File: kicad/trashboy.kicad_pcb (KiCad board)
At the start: 2 copper layers, 75 x 67 mm, 29 parts, among them J1 Conn_01x02, J2 Conn_01x07_Socket, U1 MCP23017x-x-SP, X1 TERMBLOCK_1X2

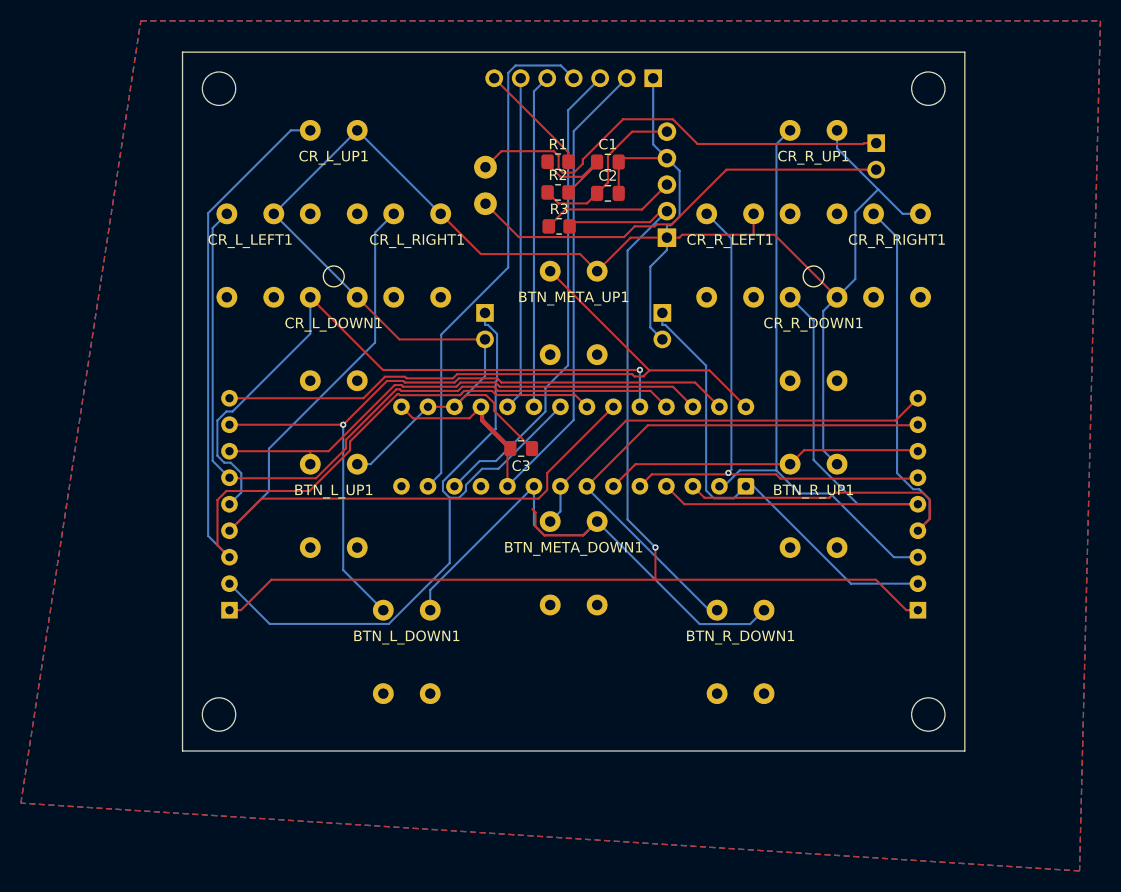
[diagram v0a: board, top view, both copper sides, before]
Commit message: Fix a few PCB issues:
1) 3v3 label issue
2) Reversed polarity on port expander.
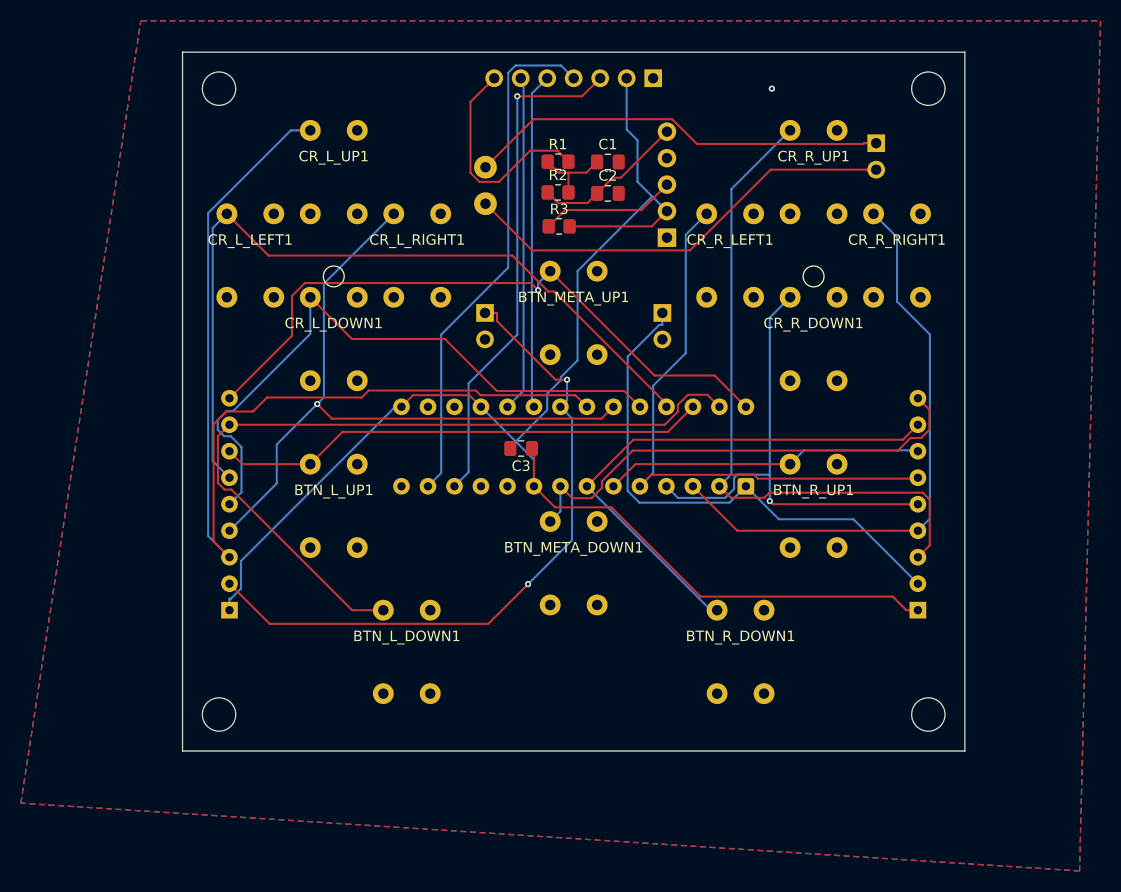
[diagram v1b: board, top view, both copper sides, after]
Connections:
- C3 pad 1: GND -> +3.3V
- C3 pad 2: +3.3V -> GND
- JP1 pad 2: +3V3 -> +3.3V
- R3 pad 2: +3V3 -> +3.3V
- RN1 pad 1: +3V3 -> +3.3V
- RN2 pad 1: +3V3 -> +3.3V
- U1 pad 10: +3.3V -> GND
- U1 pad 9: GND -> +3.3V
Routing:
- net GND: track 257.2 -> 0.00 mm, vias 0 -> 1
- net +3V3: track 116.4 -> 0.00 mm, vias 1 -> 0
- net +3.3V: track 65.2 -> 143.7 mm
- net SW2: track 79.6 -> 66.3 mm, vias 0 -> 1
- net SOUND_OUT: track 10.9 -> 21.4 mm
- net SW9: track 56.2 -> 64.0 mm
- net SW8: track 43.9 -> 51.4 mm
- net SW6: track 69.4 -> 76.0 mm, vias 1 -> 0
- net SW11: track 53.1 -> 46.6 mm, vias 0 -> 1
- net SW15: track 41.6 -> 46.2 mm
- net SW1: track 93.9 -> 98.1 mm
- net SW10: track 60.5 -> 56.4 mm
- net SW4: track 73.5 -> 76.5 mm
- net Net-(J2-Pin_3): track 45.8 -> 48.5 mm, vias 0 -> 1
- net SW7: track 65.8 -> 63.1 mm, vias 0 -> 1
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
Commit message: Fix disconnected ground plane, ready for PCB v0.2.
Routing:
- net GND: vias 1 -> 2
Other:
- board text added: "TrashBoy v0.2 - June 2026 Sascha Häberling / Arno Puder"
- board text removed: "TrashBoy v0.1 - June 2026 Sascha Häberling / Arno Puder"
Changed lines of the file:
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@@
 		)
 	)
-	(gr_text "  TrashBoy v0.1 - June 2026\nSascha Häberling / Arno Puder"
+	(gr_text "  TrashBoy v0.2 - June 2026\nSascha Häberling / Arno Puder"
 		(at 11 32.5 0)
 		(layer "B.SilkS")
@@
 	)
 	(via
+		(at 7 -25.5)
+		(size 0.6)
+		(drill 0.3)
+		(layers "F.Cu" "B.Cu")
+		(net "GND")
+	)
+	(via
